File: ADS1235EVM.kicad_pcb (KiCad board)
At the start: 2 copper layers, 50 x 25 mm, 67 parts, among them J1 Conn_01x04_Pin, J2 Conn_01x06_Pin, J3 Conn_01x05_Pin, U1 ADS1235QWRHMRQ1, U2 LM27762, U5 UCC27524DGN

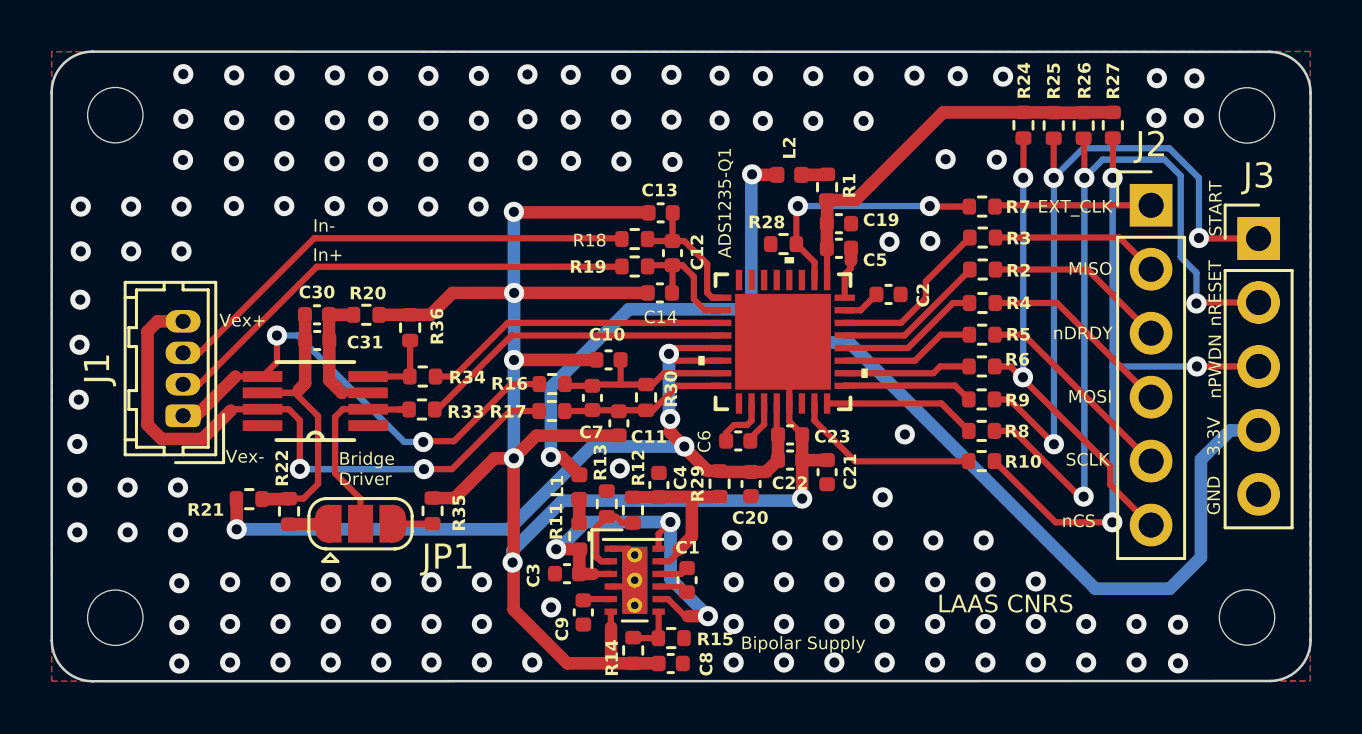
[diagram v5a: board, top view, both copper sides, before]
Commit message: KiCAD - Add of load cell measurement
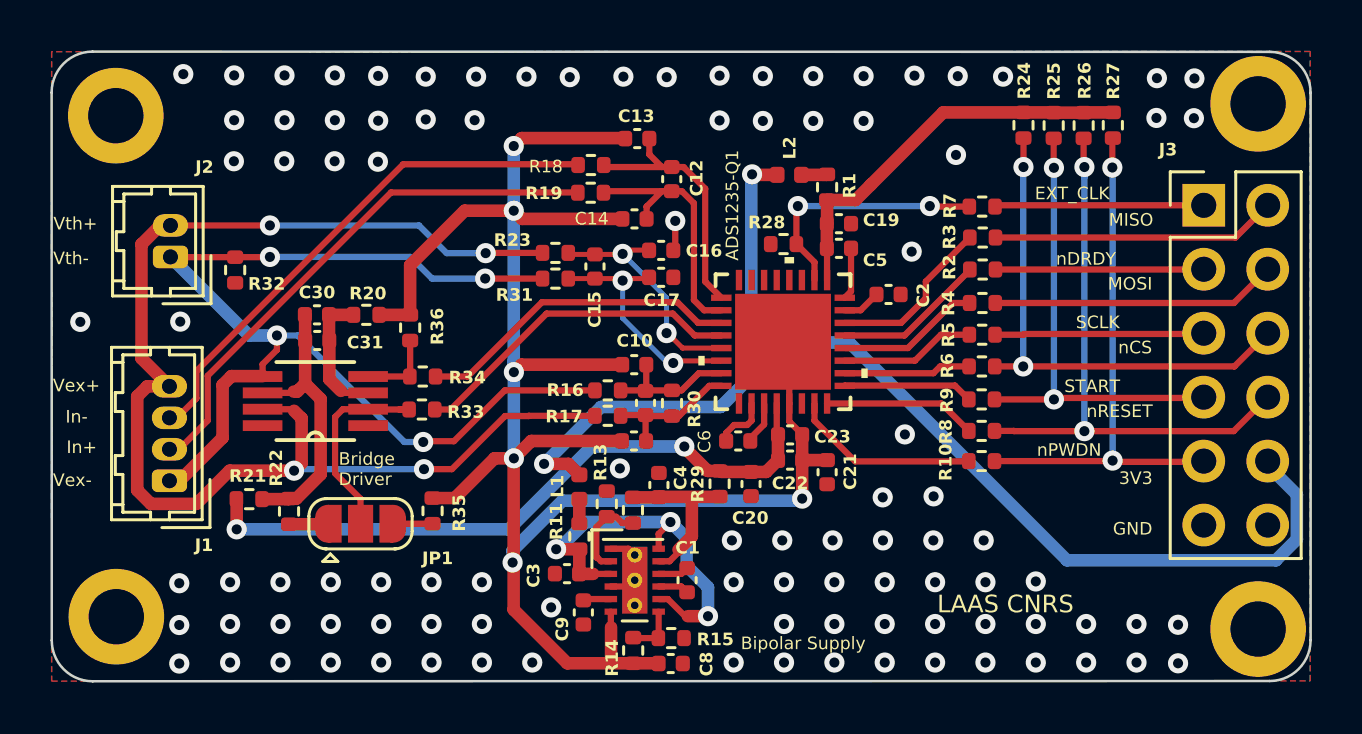
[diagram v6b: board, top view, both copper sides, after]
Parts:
- removed the REF** at (147.5, 102.5)
- removed the REF** at (102.5, 122.5)
- removed the REF** at (147.5, 122.5)
- removed the REF** at (102.5, 102.5)
- added C15: 0.1u, Capacitor_SMD:C_0402_1005Metric, F.Cu at (121.6, 108.5)
- added C16: 0.01u, Capacitor_SMD:C_0402_1005Metric, F.Cu at (124.2, 107.9)
- added C17: 0.01u, Capacitor_SMD:C_0402_1005Metric, F.Cu at (124.2, 109.0)
- added R23: 1k, Resistor_SMD:R_0402_1005Metric, F.Cu at (120.0, 108.0)
- added R31: 1k, Resistor_SMD:R_0402_1005Metric, F.Cu at (120.0, 109.0)
- added R32: 100k, Resistor_SMD:R_0402_1005Metric, F.Cu at (107.3, 108.7)
- added REF**: MountingHole_2.2mm_M2_DIN965_Pad, MountingHole:MountingHole_2.2mm_M2_DIN965_Pad, F.Cu at (147.9, 122.9)
- added REF**: MountingHole_2.2mm_M2_DIN965_Pad, MountingHole:MountingHole_2.2mm_M2_DIN965_Pad, F.Cu at (102.6, 122.4)
- added REF**: MountingHole_2.2mm_M2_DIN965_Pad, MountingHole:MountingHole_2.2mm_M2_DIN965_Pad, F.Cu at (102.5, 102.5)
- added REF**: MountingHole_2.2mm_M2_DIN965_Pad, MountingHole:MountingHole_2.2mm_M2_DIN965_Pad, F.Cu at (147.9, 102.1)
- J2: value Conn_01x06_Pin -> Conn_01x02_Pin; footprint Connector_PinHeader_2.54mm:PinHeader_1x06_P2.54mm_Vertical -> Connector_Hirose:Hirose_DF13-02P-1.25DSA_1x02_P1.25mm_Vertical
- J3: value Conn_01x05_Pin -> Conn_01x12_Pin; footprint Connector_PinHeader_2.54mm:PinHeader_1x05_P2.54mm_Vertical -> Connector_PinHeader_2.54mm:PinHeader_2x06_P2.54mm_Vertical
- moved J2 39.0 mm to (104.7, 108.2), turned to 90 degrees
- moved R18 3.42 mm to (121.4, 104.5)
- moved R19 3.41 mm to (121.4, 105.6)
- moved C14 3.11 mm to (123.2, 106.6)
- moved C13 3.09 mm to (123.3, 103.5)
- moved C12 2.94 mm to (124.6, 105.1)
- moved J1 2.64 mm to (104.7, 117.0)
- moved J3 2.55 mm to (145.8, 106.1)
- moved R17 2.23 mm to (122.1, 114.5)
- moved R16 2.22 mm to (122.1, 113.5)
- moved C7 2.12 mm to (123.6, 114.0)
- moved R30 1.06 mm to (124.6, 114.0)
- moved C10 1.04 mm to (123.1, 112.4)
- moved C11 0.92 mm to (123.1, 115.5), turned to 180 degrees
- turned R21 to 180 degrees
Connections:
- J2 pad 1: Net-(J2-Pin_1) -> Net-(J1-Pin_1)
- J2 pad 2: Net-(J2-Pin_2) -> Net-(J1-Pin_4)
- J3 pad 4: /3V3 -> Net-(J3-Pin_4)
- J3 pad 5: GND -> Net-(J3-Pin_5)
- R10 pad 2: Net-(J3-Pin_3) -> Net-(J3-Pin_9)
- R2 pad 2: Net-(J2-Pin_3) -> Net-(J3-Pin_3)
- R21 pad 1: /Avdd -> Net-(U5-VDD)
- R21 pad 2: Net-(U5-VDD) -> /Avdd
- R24 pad 2: Net-(J2-Pin_6) -> Net-(J3-Pin_6)
- R25 pad 2: Net-(J3-Pin_1) -> Net-(J3-Pin_7)
- R26 pad 2: Net-(J3-Pin_2) -> Net-(J3-Pin_8)
- R27 pad 2: Net-(J3-Pin_3) -> Net-(J3-Pin_9)
- R3 pad 2: Net-(J2-Pin_2) -> Net-(J3-Pin_2)
- R4 pad 2: Net-(J2-Pin_4) -> Net-(J3-Pin_4)
- R5 pad 2: Net-(J2-Pin_5) -> Net-(J3-Pin_5)
- R6 pad 2: Net-(J2-Pin_6) -> Net-(J3-Pin_6)
- R7 pad 2: Net-(J2-Pin_1) -> Net-(J3-Pin_1)
- R8 pad 2: Net-(J3-Pin_2) -> Net-(J3-Pin_8)
- R9 pad 2: Net-(J3-Pin_1) -> Net-(J3-Pin_7)
- U1 pad 29: /Avdd -> /Vth+
- U1 pad 30: /Avdd -> /Vth-
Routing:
- net Net-(J1-Pin_4): track 24.8 -> 52.1 mm, vias 2 -> 4
- net Net-(J1-Pin_1): track 19.1 -> 44.6 mm, vias 2 -> 4
- net Net-(J3-Pin_8): track 0.00 -> 23.5 mm, vias 0 -> 2
- net Net-(J3-Pin_9): track 0.00 -> 21.3 mm, vias 0 -> 2
- net Net-(J3-Pin_6): track 0.00 -> 20.5 mm, vias 0 -> 2
- net Net-(J3-Pin_2): track 31.1 -> 11.3 mm, vias 3 -> 0
- net Net-(J3-Pin_3): track 27.1 -> 8.18 mm, vias 3 -> 0
- net Net-(J3-Pin_1): track 27.0 -> 8.18 mm, vias 3 -> 0
- net Net-(J2-Pin_6): track 18.8 -> 0.00 mm, vias 2 -> 0
- net Net-(J3-Pin_7): track 0.00 -> 18.8 mm, vias 0 -> 2
- net Net-(J3-Pin_4): track 0.00 -> 11.4 mm
- net /Vth+: track 0.00 -> 9.68 mm, vias 0 -> 2
- net /Vth-: track 0.00 -> 9.47 mm, vias 0 -> 2
- net /Avdd: track 35.7 -> 27.3 mm, vias 4 -> 2
- net Net-(J3-Pin_5): track 0.00 -> 8.33 mm
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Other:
- board text added: "3V3"
- board text added: "Vth+"
- board text added: "Vth-"
- board text removed: "3.3V"

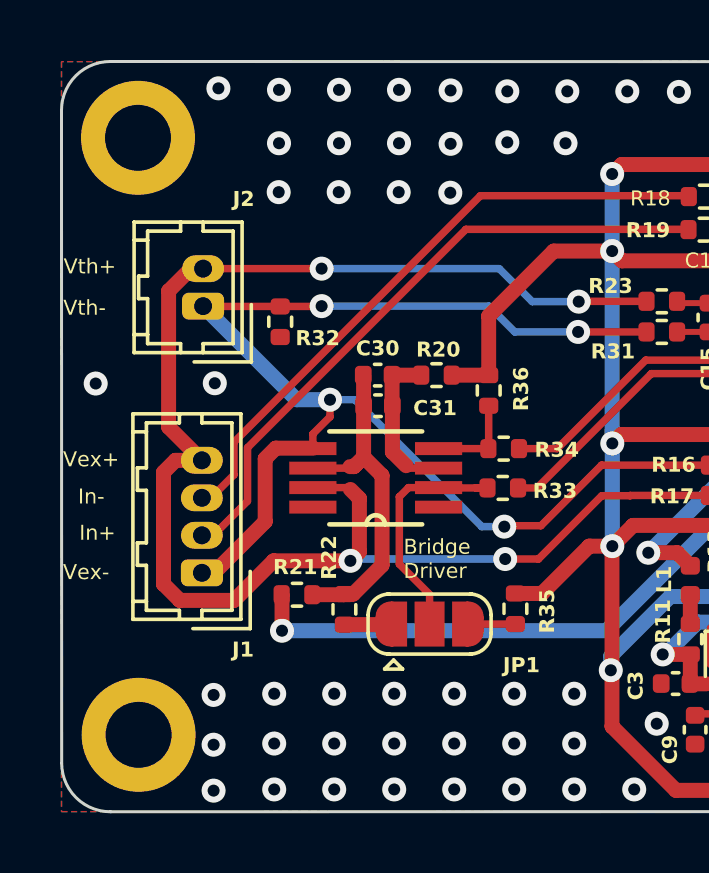
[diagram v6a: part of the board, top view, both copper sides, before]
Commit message: KiCAD - Adjustment of track width
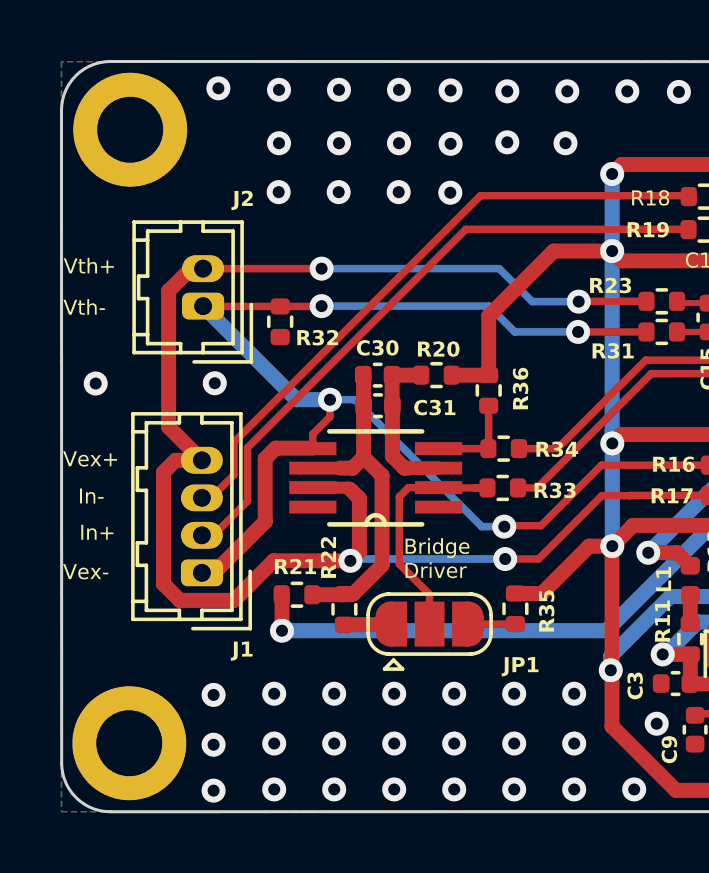
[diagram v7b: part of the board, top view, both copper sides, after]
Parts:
- moved REF** 0.42 mm to (102.3, 122.7)
- moved REF** 0.37 mm to (102.3, 102.3)
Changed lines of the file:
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@@
   )
   (footprint "MountingHole:MountingHole_2.2mm_M2_DIN965_Pad" (layer "F.Cu")
-    (at 102.57 122.44)
+    (at 102.26 122.72)
     (descr "Mounting Hole 2.2mm, M2, DIN965")
     (tags "mounting hole 2.2mm m2 din965")
@@
   )
   (footprint "MountingHole:MountingHole_2.2mm_M2_DIN965_Pad" (layer "F.Cu")
-    (at 102.55 102.54)
+    (at 102.29 102.27)
     (descr "Mounting Hole 2.2mm, M2, DIN965")
     (tags "mounting hole 2.2mm m2 din965")
@@
   (segment (start 137.49 108.65) (end 145.64 108.65) (width 0.25) (layer "F.Cu") (net 14))
   (segment (start 145.64 108.65) (end 145.62 108.67) (width 0.25) (layer "F.Cu") (net 14))
-  (segment (start 109.700002 113.549998) (end 109.81 113.44) (width 0.25) (layer "F.Cu") (net 15))
+  (segment (start 109.700002 113.549998) (end 110.07 113.18) (width 0.5) (layer "F.Cu") (net 15))
   (segment (start 108.379 113.549998) (end 109.700002 113.549998) (width 0.25) (layer "F.Cu") (net 15))
   (segment (start 110.07 113.18) (end 110.07 111.47) (width 0.5) (layer "F.Cu") (net 15))
@@
   (segment (start 108.388998 113.54) (end 108.379 113.549998) (width 0.25) (layer "F.Cu") (net 15))
   (segment (start 110.07 111.47) (end 110.07 110.46) (width 0.5) (layer "F.Cu") (net 15))
+  (segment (start 109.700002 113.549998) (end 109.29 113.549998) (width 0.5) (layer "F.Cu") (net 15))
   (segment (start 110.07 110.46) (end 110.06 110.45) (width 0.5) (layer "F.Cu") (net 15))
   (segment (start 108.36 117.77) (end 109.4075 117.77) (width 0.5) (layer "F.Cu") (net 15))
-  (segment (start 109.75 113.5) (end 109.6164 113.5) (width 0.5) (layer "F.Cu") (net 15))
   (segment (start 109.724582 117.7475) (end 109.43 117.7475) (width 0.5) (layer "F.Cu") (net 15))
   (segment (start 110.07 113.18) (end 110.685 113.795) (width 0.5) (layer "F.Cu") (net 15))
   (segment (start 109.4075 117.77) (end 109.43 117.7475) (width 0.5) (layer "F.Cu") (net 15))
-  (segment (start 109.81 113.44) (end 110.07 113.18) (width 0.5) (layer "F.Cu") (net 15))
   (segment (start 110.685 116.787082) (end 109.724582 117.7475) (width 0.5) (layer "F.Cu") (net 15))
-  (segment (start 109.81 113.44) (end 109.75 113.5) (width 0.5) (layer "F.Cu") (net 15))
   (segment (start 111.02 110.45) (end 111.02 111.46) (width 0.5) (layer "F.Cu") (net 16))
-  (segment (start 111.03 113.01) (end 111.03 111.47) (width 0.5) (layer "F.Cu") (net 16))
-  (segment (start 111.49 113.47) (end 111.03 113.01) (width 0.5) (layer "F.Cu") (net 16))
+  (segment (start 111.429949 113.55) (end 111.03 113.150051) (width 0.5) (layer "F.Cu") (net 16))
+  (segment (start 111.580002 113.549998) (end 111.58 113.55) (width 0.45) (layer "F.Cu") (net 16))
   (segment (start 111.02 110.45) (end 111.99 110.45) (width 0.5) (layer "F.Cu") (net 16))
-  (segment (start 111.49 113.47) (end 111.569998 113.549998) (width 0.25) (layer "F.Cu") (net 16))
-  (segment (start 111.569998 113.549998) (end 112.57 113.549998) (width 0.25) (layer "F.Cu") (net 16))
+  (segment (start 111.03 113.150051) (end 111.03 111.47) (width 0.5) (layer "F.Cu") (net 16))
+  (segment (start 111.58 113.55) (end 111.429949 113.55) (width 0.5) (layer "F.Cu") (net 16))
+  (segment (start 112.57 113.549998) (end 111.580002 113.549998) (width 0.45) (layer "F.Cu") (net 16))
   (segment (start 111.02 111.46) (end 111.03 111.47) (width 0.5) (layer "F.Cu") (net 16))
   (segment (start 105.75 113.77) (end 105.75 112.683604) (width 0.25) (layer "F.Cu") (net 17))
@@
   (segment (start 114.79 116.58) (end 114.79 116.43) (width 0.25) (layer "F.Cu") (net 22))
   (segment (start 103.4 117.414594) (end 103.4 113.69) (width 0.5) (layer "F.Cu") (net 22))
-  (segment (start 108.379 114.2) (end 109.57 114.2) (width 0.25) (layer "F.Cu") (net 22))
   (segment (start 109.63 116.64) (end 107.07 116.64) (width 0.5) (layer "F.Cu") (net 22))
+  (segment (start 109.93 114.56) (end 109.93 116.34) (width 0.5) (layer "F.Cu") (net 22))
   (segment (start 103.8 113.29) (end 104.81 113.29) (width 0.5) (layer "F.Cu") (net 22))
   (segment (start 117.24 108) (end 117.21 108.03) (width 0.25) (layer "F.Cu") (net 22))
@@
   (segment (start 104.72 106.9) (end 108.67 106.9) (width 0.25) (layer "F.Cu") (net 22))
   (segment (start 117.25 107.99) (end 119.5 107.99) (width 0.25) (layer "F.Cu") (net 22))
+  (segment (start 109.63 114.26) (end 109.57 114.2) (width 0.4) (layer "F.Cu") (net 22))
+  (segment (start 109.63 114.26) (end 109.93 114.56) (width 0.5) (layer "F.Cu") (net 22))
   (segment (start 104.68 113.29) (end 103.57 112.18) (width 0.5) (layer "F.Cu") (net 22))
   (segment (start 104.315406 106.9) (end 104.72 106.9) (width 0.5) (layer "F.Cu") (net 22))
   (segment (start 103.943806 117.9584) (end 103.4 117.414594) (width 0.5) (layer "F.Cu") (net 22))
+  (segment (start 109.57 114.2) (end 108.379 114.2) (width 0.4) (layer "F.Cu") (net 22))
   (segment (start 107.07 116.64) (end 105.7516 117.9584) (width 0.5) (layer "F.Cu") (net 22))
-  (segment (start 109.57 114.2) (end 109.63 114.26) (width 0.25) (layer "F.Cu") (net 22))
   (segment (start 105.7516 117.9584) (end 103.943806 117.9584) (width 0.5) (layer "F.Cu") (net 22))
+  (segment (start 108.67 106.9) (end 108.63 106.9) (width 0.25) (layer "F.Cu") (net 22))
+  (segment (start 115.9 116.58) (end 114.79 116.58) (width 0.25) (layer "F.Cu") (net 22))
   (segment (start 109.93 116.34) (end 109.63 116.64) (width 0.5) (layer "F.Cu") (net 22))
-  (segment (start 108.67 106.9) (end 108.63 106.9) (width 0.25) (layer "F.Cu") (net 22))
-  (segment (start 109.93 114.56) (end 109.93 116.34) (width 0.5) (layer "F.Cu") (net 22))
-  (segment (start 115.9 116.58) (end 114.79 116.58) (width 0.25) (layer "F.Cu") (net 22))
-  (segment (start 109.63 114.26) (end 109.93 114.56) (width 0.5) (layer "F.Cu") (net 22))
   (via (at 117.24 108) (size 0.8) (drill 0.4) (layers "F.Cu" "B.Cu") (net 22))
   (via (at 109.63 116.64) (size 0.8) (drill 0.4) (layers "F.Cu" "B.Cu") (net 22))
